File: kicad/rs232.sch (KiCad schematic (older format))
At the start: 16 parts, among them J7 XCVR_CAT_RS232, U8 MAX3387ECUG+

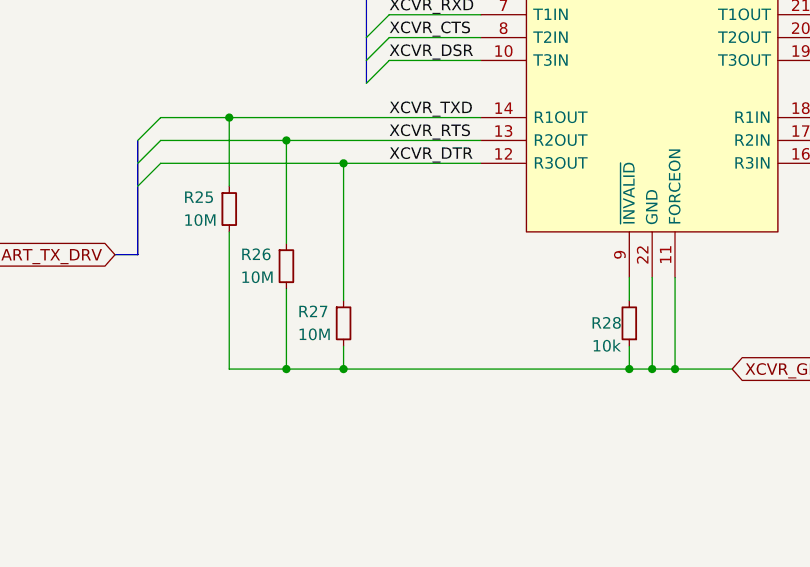
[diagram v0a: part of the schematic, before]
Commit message: Connector and pull down resistors
* Changed back to USB-B connector.
* Changed value of pull down resistors to 1k.
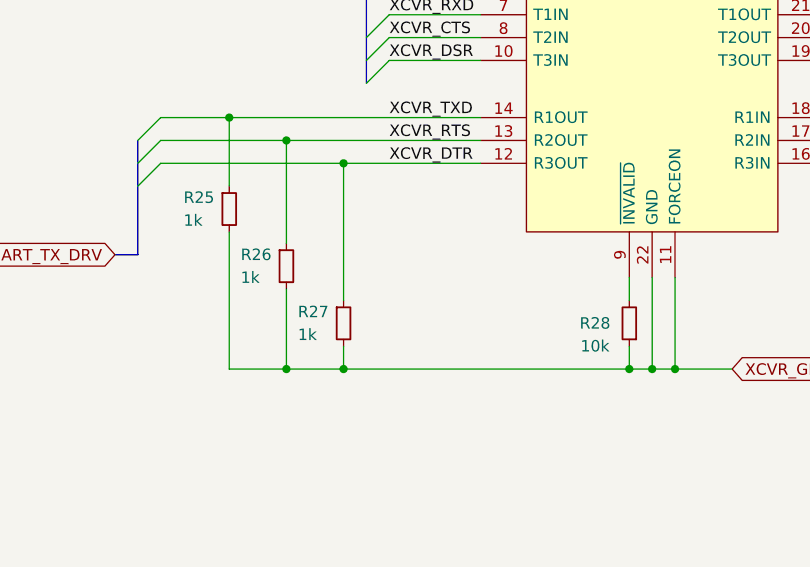
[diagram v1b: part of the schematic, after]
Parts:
- R25, R26, R27: value 10M -> 1k
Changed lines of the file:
@@
 AR Path="/5F9E7705/6072AD1D" Ref="R?"  Part="1"
 AR Path="/5F9E7705/606D9B1D/6072AD1D" Ref="R28"  Part="1"
-F 0 "R28" H 5250 4200 50  0000 C CNN
-F 1 "10k" H 5250 4300 50  0000 C CNN
+F 0 "R28" H 5300 4200 50  0000 C CNN
+F 1 "10k" H 5300 4300 50  0000 C CNN
 F 2 "" H 5150 4200 50  0001 C CNN
 F 3 "~" H 5150 4200 50  0001 C CNN
@@
 P 3400 3700
 F 0 "R25" H 3200 3750 50  0000 L CNN
-F 1 "10M" H 3200 3650 50  0000 L CNN
+F 1 "1k" H 3200 3650 50  0000 L CNN
 F 2 "" H 3400 3700 50  0001 C CNN
 F 3 "~" H 3400 3700 50  0001 C CNN
@@
 P 3650 3950
 F 0 "R26" H 3450 4000 50  0000 L CNN
-F 1 "10M" H 3450 3900 50  0000 L CNN
+F 1 "1k" H 3450 3900 50  0000 L CNN
 F 2 "" H 3650 3950 50  0001 C CNN
 F 3 "~" H 3650 3950 50  0001 C CNN
@@
 P 3900 4200
 F 0 "R27" H 3700 4250 50  0000 L CNN
-F 1 "10M" H 3700 4150 50  0000 L CNN
+F 1 "1k" H 3700 4150 50  0000 L CNN
 F 2 "" H 3900 4200 50  0001 C CNN
 F 3 "~" H 3900 4200 50  0001 C CNN

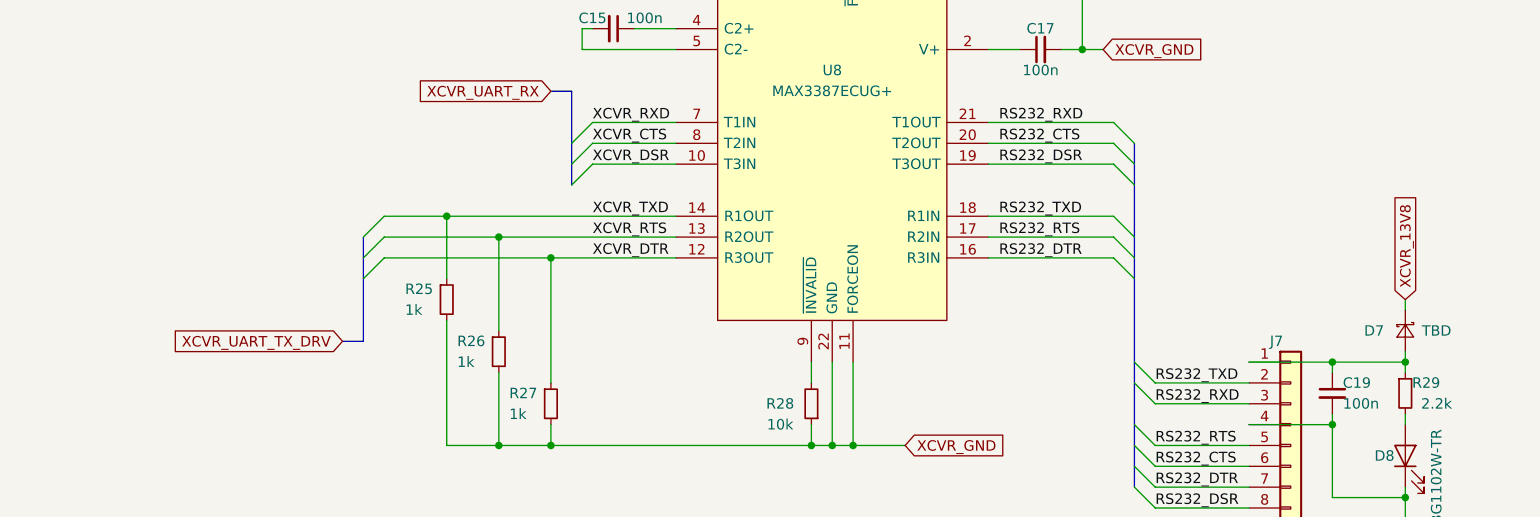
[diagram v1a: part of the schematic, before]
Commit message: Initial footprint placement + changes
* Added initial placement
* Remove pull-down resistors from USB lines.
* Remove ferrite bead from FTDI chip as it was very close to Vcc FB
* Fixed MAX TX pins
* Assigned footprints.
* Removed redundant solder jumpers.
* Small changes for layout coherence.
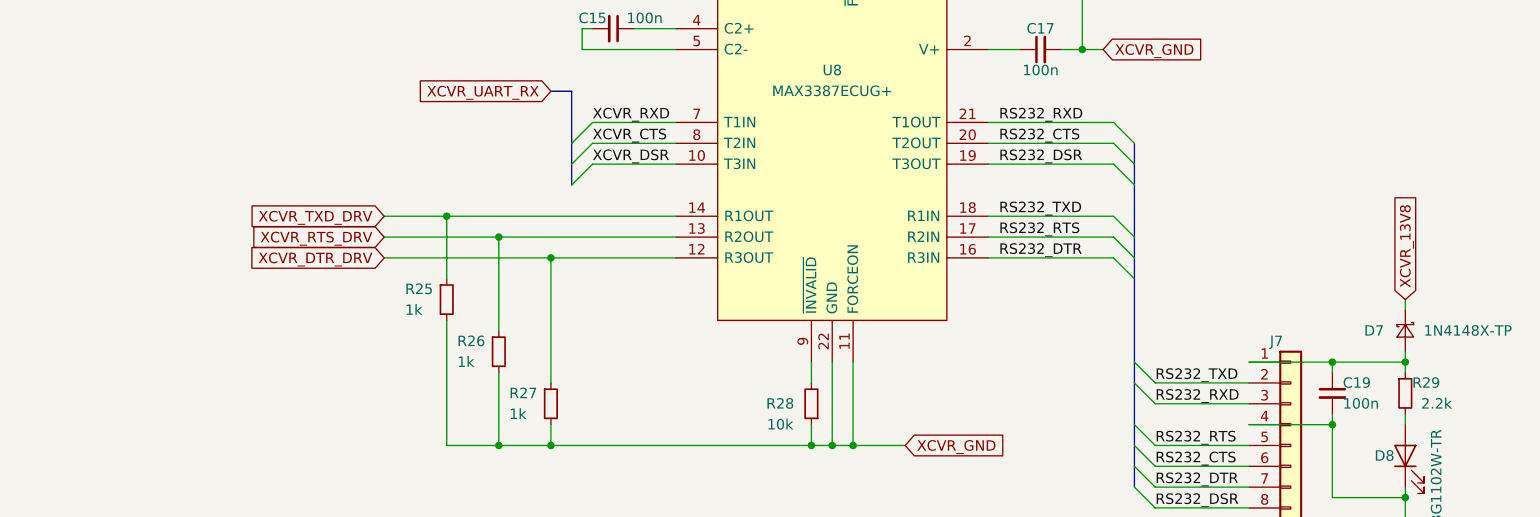
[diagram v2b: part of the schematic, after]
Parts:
- C14, C15, C16, C17, C18, C19: footprint (none) -> Capacitor_SMD:C_1206_3216Metric_Pad1.42x1.75mm_HandSolder
- D7: value TBD -> 1N4148X-TP; footprint (none) -> Diode_SMD:D_SOD-523
- D8: footprint (none) -> LED_SMD:LED_1206_3216Metric_Pad1.42x1.75mm_HandSolder
- FB6: footprint (none) -> Inductor_SMD:L_1206_3216Metric_Pad1.42x1.75mm_HandSolder
- J7: footprint (none) -> custom:TB003-500-P08BE
- R25, R26, R27, R28, R29: footprint (none) -> Resistor_SMD:R_1206_3216Metric_Pad1.42x1.75mm_HandSolder
- U8: footprint SOP65P640X110-24N -> Package_SO:TSSOP-24_4.4x7.8mm_P0.65mm
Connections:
- net XCVR_DTR renamed XCVR_DTR_DRV
- net XCVR_RTS renamed XCVR_RTS_DRV
- net XCVR_TXD renamed XCVR_TXD_DRV
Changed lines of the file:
@@
 F 0 "C16" V 6350 2100 50  0000 C CNN
 F 1 "100n" V 6150 2100 50  0000 C CNN
-F 2 "" H 6250 2100 50  0001 C CNN
+F 2 "Capacitor_SMD:C_1206_3216Metric_Pad1.42x1.75mm_HandSolder" H 6250 2100 50  0001 C CNN
 F 3 "~" H 6250 2100 50  0001 C CNN
 	1    6250 2100
@@
 F 0 "C17" V 6350 2500 50  0000 C CNN
 F 1 "100n" V 6150 2500 50  0000 C CNN
-F 2 "" H 6250 2500 50  0001 C CNN
+F 2 "Capacitor_SMD:C_1206_3216Metric_Pad1.42x1.75mm_HandSolder" H 6250 2500 50  0001 C CNN
 F 3 "~" H 6250 2500 50  0001 C CNN
 	1    6250 2500
@@
 F 0 "U8" H 5250 1600 50  0000 C CNN
 F 1 "MAX3387ECUG+" H 5250 1500 50  0000 C CNN
-F 2 "SOP65P640X110-24N" H 7900 2100 50  0001 L CNN
+F 2 "Package_SO:TSSOP-24_4.4x7.8mm_P0.65mm" H 7900 2100 50  0001 L CNN
 F 3 "" H 6300 2700 50  0001 L CNN
 F 4 "MAX3387ECUG+, Multichannel Line Transceiver, EIA/TIA-232, RS-232, V.24, V.28 3 3 3 250kbit/s, 3  5.5 V, 24-Pin" H 7850 1750 50  0001 L CNN "Description"
@@
 F 0 "C14" V 4150 2000 50  0000 C CNN
 F 1 "100n" V 4150 2250 50  0000 C CNN
-F 2 "" H 4200 2100 50  0001 C CNN
+F 2 "Capacitor_SMD:C_1206_3216Metric_Pad1.42x1.75mm_HandSolder" H 4200 2100 50  0001 C CNN
 F 3 "~" H 4200 2100 50  0001 C CNN
 	1    4200 2100
@@
 F 0 "C15" V 4150 2300 50  0000 C CNN
 F 1 "100n" V 4150 2550 50  0000 C CNN
-F 2 "" H 4200 2400 50  0001 C CNN
+F 2 "Capacitor_SMD:C_1206_3216Metric_Pad1.42x1.75mm_HandSolder" H 4200 2400 50  0001 C CNN
 F 3 "~" H 4200 2400 50  0001 C CNN
 	1    4200 2400
@@
 Wire Wire Line
 	4100 2950 4500 2950
-Wire Wire Line
-	4100 3050 4500 3050
 Text Label 4100 2850 0    50   ~ 0
 XCVR_RXD
@@
 F 0 "J7" H 7350 4700 50  0000 L CNN
 F 1 "XCVR_CAT_RS232" H 6900 3800 50  0000 L CNN
-F 2 "" H 7450 4300 50  0001 C CNN
+F 2 "custom:TB003-500-P08BE" H 7450 4300 50  0001 C CNN
 F 3 "~" H 7450 4300 50  0001 C CNN
 	1    7450 4300
@@
 F 0 "C18" H 6300 1900 50  0000 C CNN
 F 1 "100n" H 6300 2000 50  0000 C CNN
-F 2 "" H 6450 1900 50  0001 C CNN
+F 2 "Capacitor_SMD:C_1206_3216Metric_Pad1.42x1.75mm_HandSolder" H 6450 1900 50  0001 C CNN
 F 3 "~" H 6450 1900 50  0001 C CNN
 	1    6450 1900
@@
 F 0 "C19" H 7700 4200 50  0000 L CNN
 F 1 "100n" H 7700 4100 50  0000 L CNN
-F 2 "" H 7650 4150 50  0001 C CNN
+F 2 "Capacitor_SMD:C_1206_3216Metric_Pad1.42x1.75mm_HandSolder" H 7650 4150 50  0001 C CNN
 F 3 "~" H 7650 4150 50  0001 C CNN
 	1    7650 4150
@@
 F 0 "R28" H 5300 4200 50  0000 C CNN
 F 1 "10k" H 5300 4300 50  0000 C CNN
-F 2 "" H 5150 4200 50  0001 C CNN
+F 2 "Resistor_SMD:R_1206_3216Metric_Pad1.42x1.75mm_HandSolder" H 5150 4200 50  0001 C CNN
 F 3 "~" H 5150 4200 50  0001 C CNN
 	1    5150 4200
@@
 F 0 "FB6" V 6700 1750 50  0000 C CNN
 F 1 "Fe" V 6550 1600 50  0000 C CNN
-F 2 "" V 6580 1650 50  0001 C CNN
+F 2 "Inductor_SMD:L_1206_3216Metric_Pad1.42x1.75mm_HandSolder" V 6580 1650 50  0001 C CNN
 F 3 "~" H 6650 1650 50  0001 C CNN
 	1    6650 1650
@@
 AR Path="/5F9E7705/606D9B1D/6072AD2D" Ref="D7"  Part="1"
 F 0 "D7" V 8000 3700 50  0000 C CNN
-F 1 "TBD" V 8000 4000 50  0000 C CNN
-F 2 "" V 8000 3850 50  0001 C CNN
+F 1 "1N4148X-TP" V 8000 4150 50  0000 C CNN
+F 2 "Diode_SMD:D_SOD-523" V 8000 3850 50  0001 C CNN
 F 3 "~" V 8000 3850 50  0001 C CNN
 	1    8000 3850
@@
 F 0 "R29" H 8100 4200 50  0000 C CNN
 F 1 "2.2k" H 8150 4100 50  0000 C CNN
-F 2 "" H 8000 4150 50  0001 C CNN
+F 2 "Resistor_SMD:R_1206_3216Metric_Pad1.42x1.75mm_HandSolder" H 8000 4150 50  0001 C CNN
 F 3 "~" H 8000 4150 50  0001 C CNN
 	1    8000 4150
@@
 F 0 "D8" V 8000 4550 50  0000 C CNN
 F 1 "BG1102W-TR" H 7900 4300 50  0000 C CNN
-F 2 "" H 8000 4450 50  0001 C CNN
+F 2 "LED_SMD:LED_1206_3216Metric_Pad1.42x1.75mm_HandSolder" H 8000 4450 50  0001 C CNN
 F 3 "~" H 8000 4450 50  0001 C CNN
 	1    8000 4450
@@
 	8000 4800 8000 4650
 Connection ~ 8000 4650
-Text GLabel 2900 3900 0    50   Input ~ 0
-XCVR_UART_TX_DRV
-Wire Bus Line
-	2900 3900 3000 3900
-Entry Wire Line
-	3000 3400 3100 3300
-Entry Wire Line
-	3000 3500 3100 3400
-Entry Wire Line
-	3000 3600 3100 3500
-Text Label 4100 3300 0    50   ~ 0
-XCVR_TXD
-Text Label 4100 3400 0    50   ~ 0
-XCVR_RTS
-Text Label 4100 3500 0    50   ~ 0
-XCVR_DTR
 Connection ~ 7650 4000
 $Comp
@@
 F 0 "R25" H 3200 3750 50  0000 L CNN
 F 1 "1k" H 3200 3650 50  0000 L CNN
-F 2 "" H 3400 3700 50  0001 C CNN
+F 2 "Resistor_SMD:R_1206_3216Metric_Pad1.42x1.75mm_HandSolder" H 3400 3700 50  0001 C CNN
 F 3 "~" H 3400 3700 50  0001 C CNN
 	1    3400 3700
@@
 F 0 "R26" H 3450 4000 50  0000 L CNN
 F 1 "1k" H 3450 3900 50  0000 L CNN
-F 2 "" H 3650 3950 50  0001 C CNN
+F 2 "Resistor_SMD:R_1206_3216Metric_Pad1.42x1.75mm_HandSolder" H 3650 3950 50  0001 C CNN
 F 3 "~" H 3650 3950 50  0001 C CNN
 	1    3650 3950
@@
 F 0 "R27" H 3700 4250 50  0000 L CNN
 F 1 "1k" H 3700 4150 50  0000 L CNN
-F 2 "" H 3900 4200 50  0001 C CNN
+F 2 "Resistor_SMD:R_1206_3216Metric_Pad1.42x1.75mm_HandSolder" H 3900 4200 50  0001 C CNN
 F 3 "~" H 3900 4200 50  0001 C CNN
 	1    3900 4200
@@
 $EndComp
 Wire Wire Line
-	3100 3300 3400 3300
-Wire Wire Line
-	3100 3400 3650 3400
-Wire Wire Line
-	3100 3500 3900 3500
-Wire Wire Line
 	5150 4400 3900 4400
 Connection ~ 5150 4400
@@
 	5350 4400 5600 4400
 Connection ~ 5350 4400
+Wire Wire Line
+	4500 3050 4100 3050
+Text GLabel 3100 3300 0    50   Input ~ 0
+XCVR_TXD_DRV
+Text GLabel 3100 3400 0    50   Input ~ 0
+XCVR_RTS_DRV
+Text GLabel 3100 3500 0    50   Input ~ 0
+XCVR_DTR_DRV
 Wire Bus Line
 	4000 2700 4000 3150
 Wire Bus Line
-	3000 3400 3000 3900
-Wire Bus Line
 	6700 2950 6700 4600
+Wire Wire Line
+	3100 3300 3400 3300
+Wire Wire Line
+	3100 3400 3650 3400
+Wire Wire Line
+	3100 3500 3900 3500
 $EndSCHEMATC

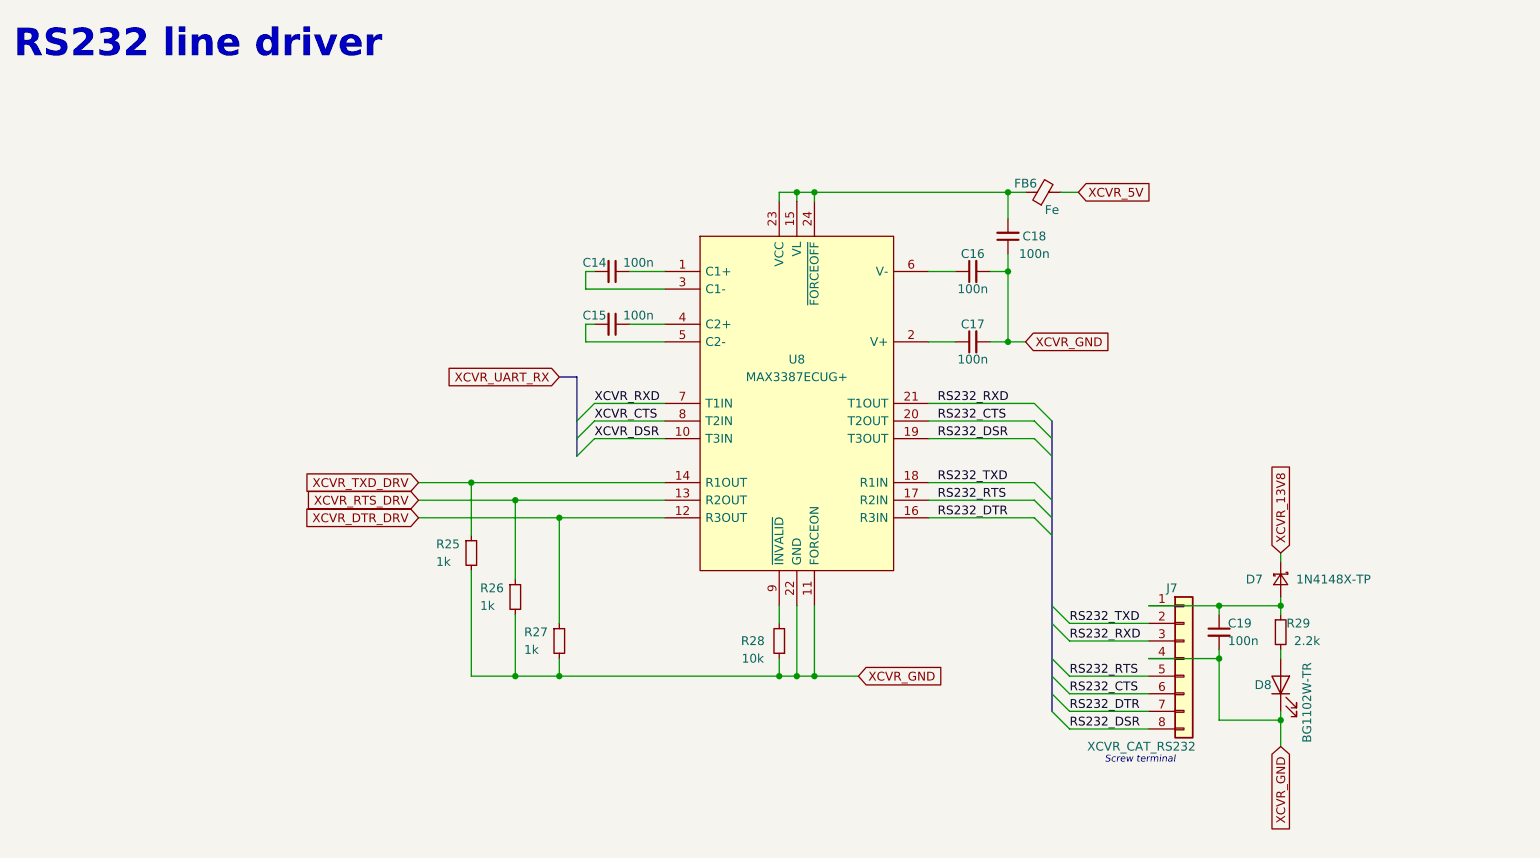
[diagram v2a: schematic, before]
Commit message: New layout, routing, misc...
* Redo layout
* Fixed MAX pulldown resistors on data lines.
* Added jumpers in case MAX not installed.
* Remove audio header
* Remove some redundant solder jumpers
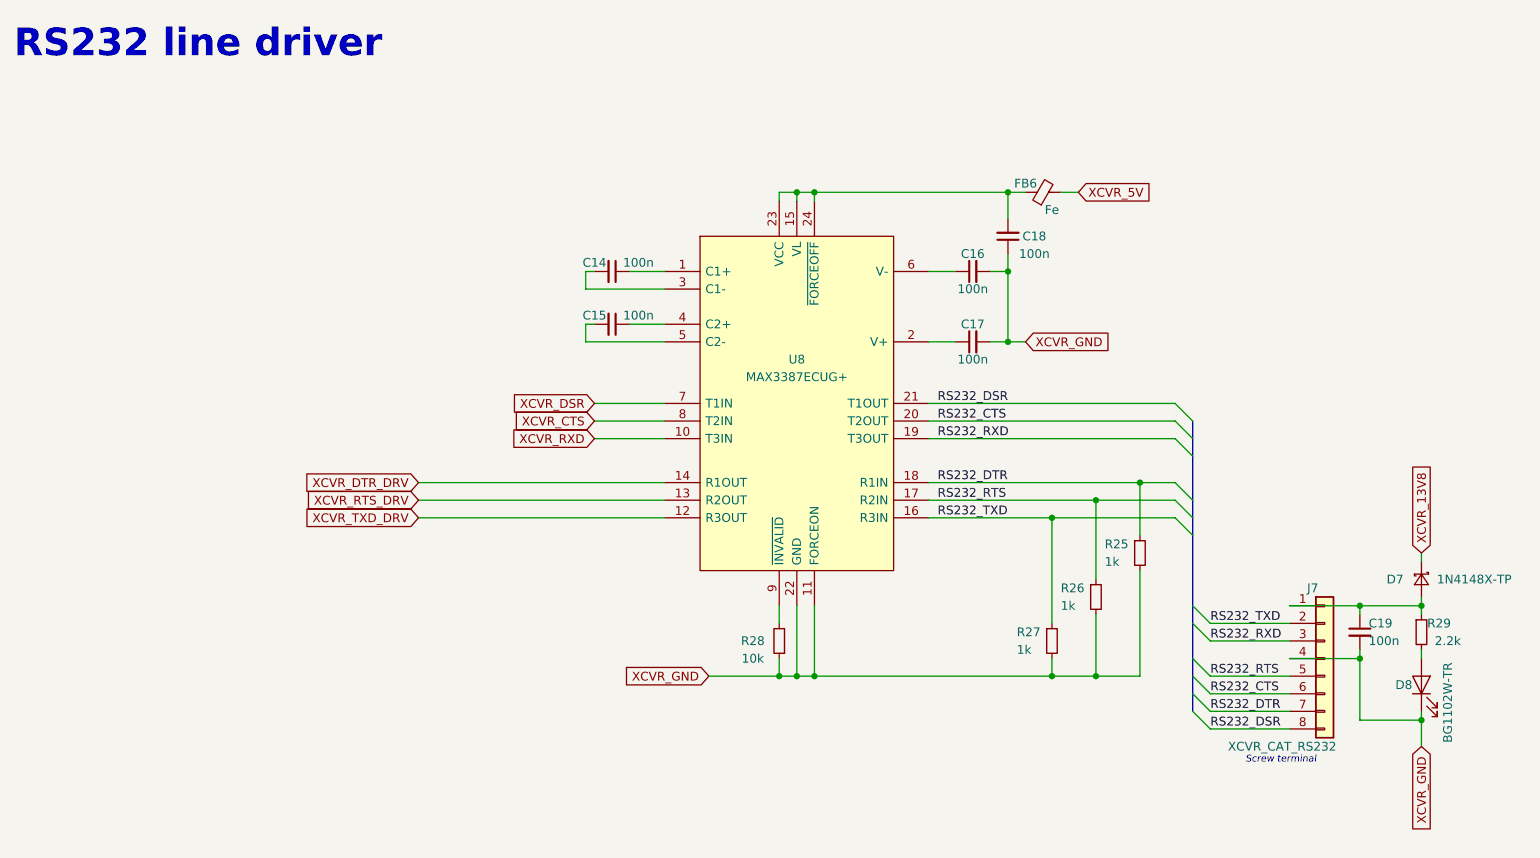
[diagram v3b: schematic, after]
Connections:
- net RS232_DSR: now also U8.21 (T1OUT); no longer U8.19 (T3OUT)
- net RS232_DTR: now also R25.1, U8.18 (R1IN); no longer U8.16 (R3IN)
- net RS232_RTS: now also R26.1
- net RS232_RXD: now also U8.19 (T3OUT); no longer U8.21 (T1OUT)
- net RS232_TXD: now also R27.1, U8.16 (R3IN); no longer U8.18 (R1IN)
- net XCVR_DSR: now also U8.7 (T1IN); no longer U8.10 (T3IN)
- net XCVR_DTR_DRV: now also U8.14 (R1OUT); no longer R27.1, U8.12 (R3OUT)
- net XCVR_RTS_DRV: no longer R26.1
- net XCVR_RXD: now also U8.10 (T3IN); no longer U8.7 (T1IN)
- net XCVR_TXD_DRV: now also U8.12 (R3OUT); no longer R25.1, U8.14 (R1OUT)
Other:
- moved on the sheet: C19, D7, D8, J7, R25, R26, R27, R29

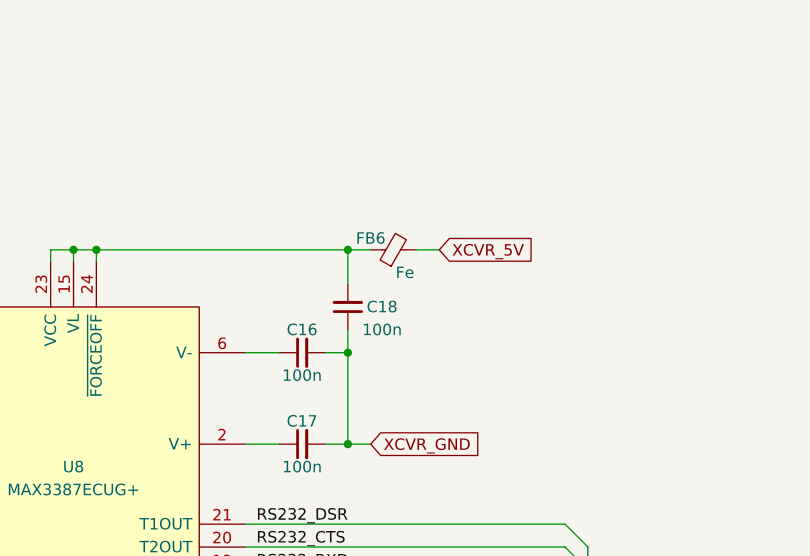
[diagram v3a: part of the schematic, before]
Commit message: Ferrite beads, hacking pads, audio fix
* Chose ferrite beads for IC Vcc (BLM31KN102SH1L)
* Change hacking pad thickness to 0.8mm
* Fixed potential oscillator when grounding audio- lines
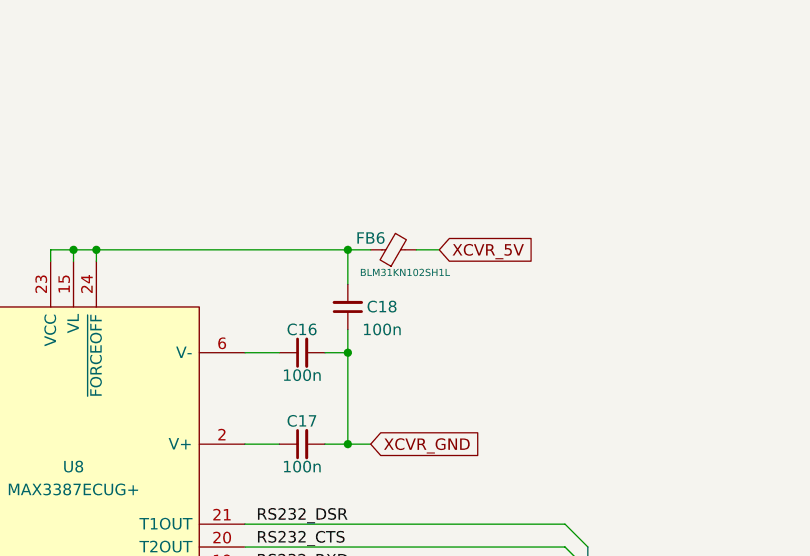
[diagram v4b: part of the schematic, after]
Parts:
- FB6: value Fe -> BLM31KN102SH1L
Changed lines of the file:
@@
 AR Path="/5F9E7705/606D9B1D/6072AD26" Ref="FB6"  Part="1"
 F 0 "FB6" V 6700 1750 50  0000 C CNN
-F 1 "Fe" V 6550 1600 50  0000 C CNN
+F 1 "BLM31KN102SH1L" V 6550 1600 31  0000 C CNN
 F 2 "Inductor_SMD:L_1206_3216Metric_Pad1.42x1.75mm_HandSolder" V 6580 1650 50  0001 C CNN
 F 3 "~" H 6650 1650 50  0001 C CNN
@@
 Wire Wire Line
 	4750 4400 5150 4400
+Connection ~ 5150 4400
 Wire Bus Line
 	7500 2950 7500 4600
-Connection ~ 5150 4400
 $EndSCHEMATC
